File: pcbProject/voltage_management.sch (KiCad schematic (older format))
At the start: 2 parts, among them U3 LP2985-33DBVR

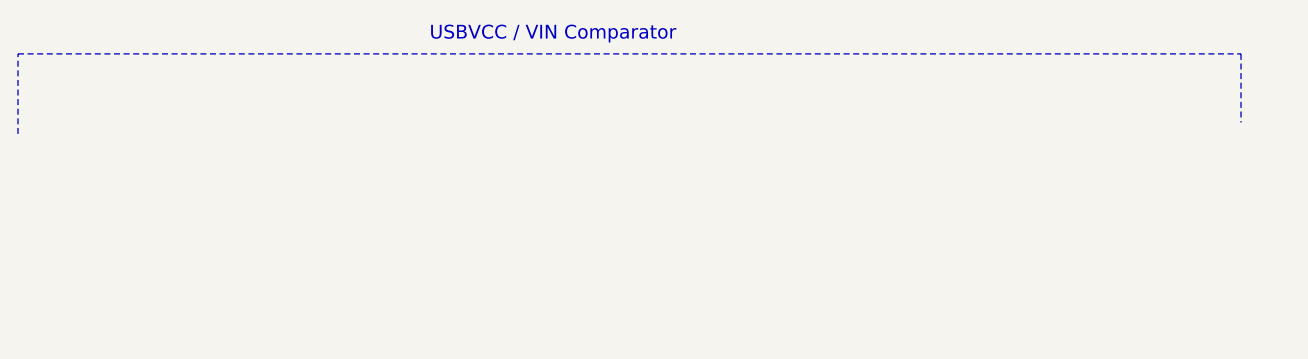
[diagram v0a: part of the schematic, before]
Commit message: bestellijst+pcbvoltageregulator aangepast
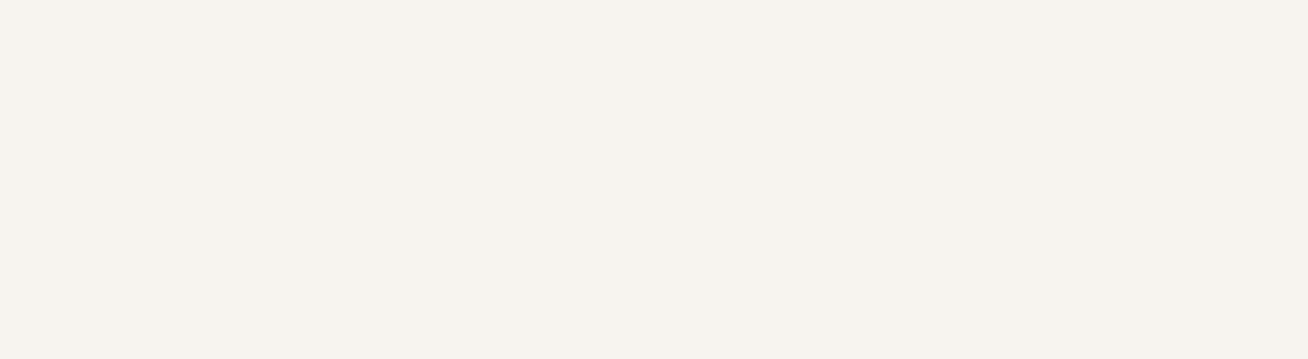
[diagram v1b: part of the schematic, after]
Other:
- note removed: "USBVCC / VIN Comparator"
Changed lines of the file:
@@
 	8000 4750 8000 5325
 Connection ~ 8000 4200
-Wire Notes Line
-	2650 2500 2650 2150
-Wire Notes Line
-	2650 2150 8000 2150
-Wire Notes Line
-	8000 2150 8000 2450
 Wire Wire Line
 	5400 3700 5400 4200
-Text Notes 4450 2100 0    60   ~ 0
-USBVCC / VIN Comparator
 $Comp
 L Arduino_Uno_R3_From_Scratch:3V3_LDO #PWR013

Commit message: deel1routingpcb
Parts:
- C6: value 2.2uF -> 1uF; footprint ~ -> Capacitor_SMD:C_1206_3216Metric
- U3: footprint ~ -> LP2985-33DBVR:SOT95P280X145-5N
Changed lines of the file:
@@
 F 0 "U3" H 7200 4050 60  0000 C CNN
 F 1 "LP2985-33DBVR" H 7000 4950 60  0000 C CNN
-F 2 "~" H 7000 4500 60  0000 C CNN
+F 2 "LP2985-33DBVR:SOT95P280X145-5N" H 7000 4500 60  0000 C CNN
 F 3 "http://www.ti.com/lit/ds/symlink/lp2985-33.pdf" H 7000 4500 60  0001 C CNN
 F 4 "3.3V FIXED POSITIVE LDO REGULATOR, 0.575V DROPOUT" H 7000 4500 60  0001 C CNN "Characteristics"
@@
 P 8000 4600
 F 0 "C6" H 8000 4700 40  0000 L CNN
-F 1 "2.2uF" H 8006 4515 40  0000 L CNN
-F 2 "~" H 8038 4450 30  0000 C CNN
+F 1 "1uF" H 8006 4515 40  0000 L CNN
+F 2 "Capacitor_SMD:C_1206_3216Metric" H 8038 4450 30  0000 C CNN
 F 3 "http://product.tdk.com/en/catalog/datasheets/mlcc_commercial_general_en.pdf" H 8000 4600 60  0001 C CNN
 F 4 "CAP CER 2.2UF 16V X7R 0805" H 8000 4600 60  0001 C CNN "Characteristics"

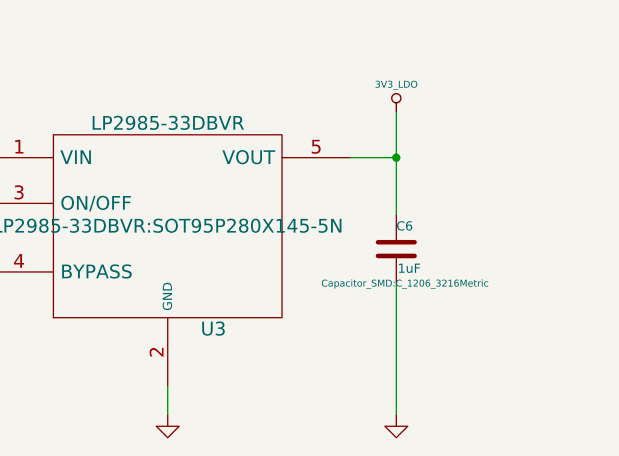
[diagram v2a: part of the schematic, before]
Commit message: PCB versie3
Aanpassingen tips coach --> veel gewijzigd
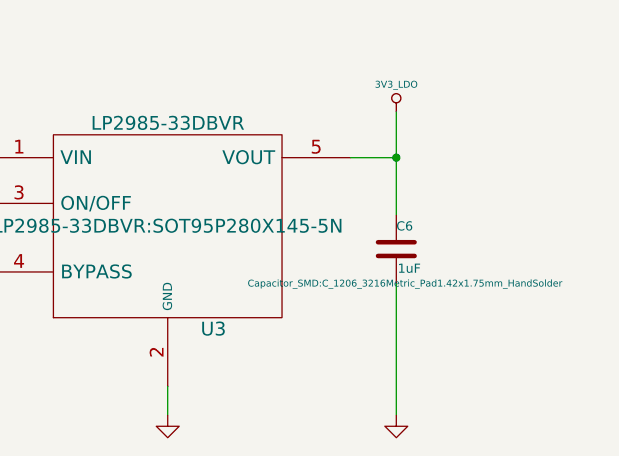
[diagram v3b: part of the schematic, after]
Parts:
- C6: footprint Capacitor_SMD:C_1206_3216Metric -> Capacitor_SMD:C_1206_3216Metric_Pad1.42x1.75mm_HandSolder
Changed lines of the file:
@@
 F 0 "C6" H 8000 4700 40  0000 L CNN
 F 1 "1uF" H 8006 4515 40  0000 L CNN
-F 2 "Capacitor_SMD:C_1206_3216Metric" H 8038 4450 30  0000 C CNN
+F 2 "Capacitor_SMD:C_1206_3216Metric_Pad1.42x1.75mm_HandSolder" H 8038 4450 30  0000 C CNN
 F 3 "http://product.tdk.com/en/catalog/datasheets/mlcc_commercial_general_en.pdf" H 8000 4600 60  0001 C CNN
 F 4 "CAP CER 2.2UF 16V X7R 0805" H 8000 4600 60  0001 C CNN "Characteristics"

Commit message: verslag
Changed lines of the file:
@@
 F 0 "U3" H 7200 4050 60  0000 C CNN
 F 1 "LP2985-33DBVR" H 7000 4950 60  0000 C CNN
-F 2 "LP2985-33DBVR:SOT95P280X145-5N" H 7000 4500 60  0000 C CNN
+F 2 "LP2985-33DBVR:SOT95P280X145-5N" H 9700 4675 60  0000 C CNN
 F 3 "http://www.ti.com/lit/ds/symlink/lp2985-33.pdf" H 7000 4500 60  0001 C CNN
 F 4 "3.3V FIXED POSITIVE LDO REGULATOR, 0.575V DROPOUT" H 7000 4500 60  0001 C CNN "Characteristics"
@@
 F 0 "C6" H 8000 4700 40  0000 L CNN
 F 1 "1uF" H 8006 4515 40  0000 L CNN
-F 2 "Capacitor_SMD:C_1206_3216Metric_Pad1.42x1.75mm_HandSolder" H 8038 4450 30  0000 C CNN
+F 2 "Capacitor_SMD:C_1206_3216Metric_Pad1.42x1.75mm_HandSolder" H 9350 4650 30  0000 C CNN
 F 3 "http://product.tdk.com/en/catalog/datasheets/mlcc_commercial_general_en.pdf" H 8000 4600 60  0001 C CNN
 F 4 "CAP CER 2.2UF 16V X7R 0805" H 8000 4600 60  0001 C CNN "Characteristics"
